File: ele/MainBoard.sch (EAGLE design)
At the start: 120 parts, among them IC1 MCP23017SP, IC2 74HC595D, IC3 74HC595D, X1 POWER_IN, X2 POWER_OUT

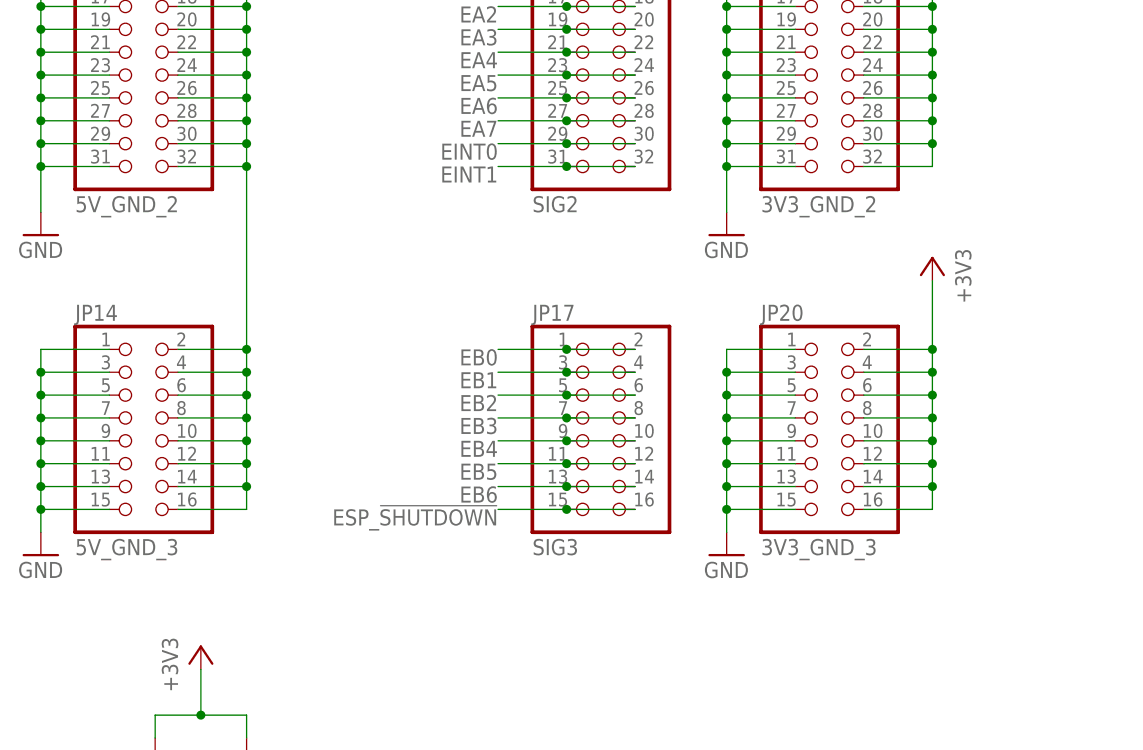
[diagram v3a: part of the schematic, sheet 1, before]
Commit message: ele: Remove impossible headers, route signals
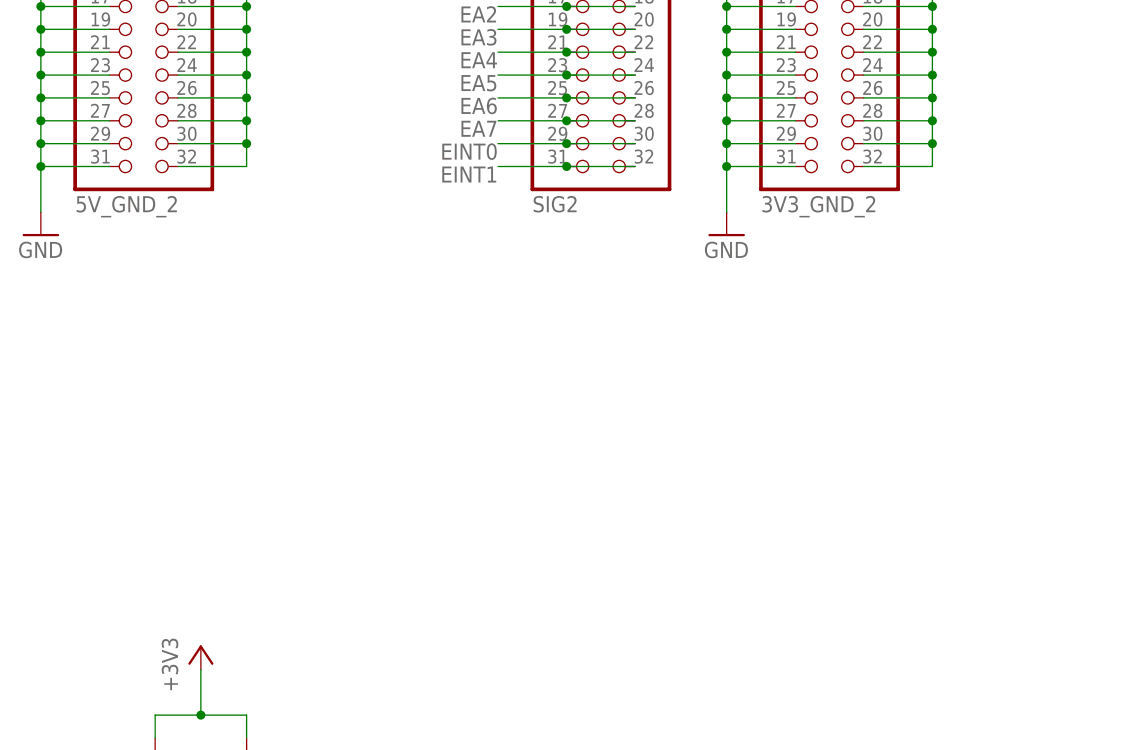
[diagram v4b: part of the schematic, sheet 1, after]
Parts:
- removed JP14: 5V_GND_3, pinhead:PINHD-2X8
- removed JP17: SIG3, pinhead:PINHD-2X8
- removed JP20: 3V3_GND_3, pinhead:PINHD-2X8
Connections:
- net +3V3: no longer JP20.10, JP20.12, JP20.14, JP20.16, JP20.2, JP20.4, JP20.6, JP20.8
- net 5V_2: no longer JP14.10, JP14.12, JP14.14, JP14.16, JP14.2, JP14.4, JP14.6, JP14.8
- net EB0: no longer JP17.1, JP17.2
- net EB1: no longer JP17.3, JP17.4
- net EB2: no longer JP17.5, JP17.6
- net EB3: no longer JP17.7, JP17.8
- net EB4: no longer JP17.10, JP17.9
- net EB5: no longer JP17.11, JP17.12
- net EB6: no longer JP17.13, JP17.14
- net ESP_!SHUTDOWN: no longer JP17.15, JP17.16
- net GND: no longer JP14.1, JP14.11, JP14.13, JP14.15, JP14.3, JP14.5, JP14.7, JP14.9, JP20.1, JP20.11, JP20.13, JP20.15, JP20.3, JP20.5, JP20.7, JP20.9

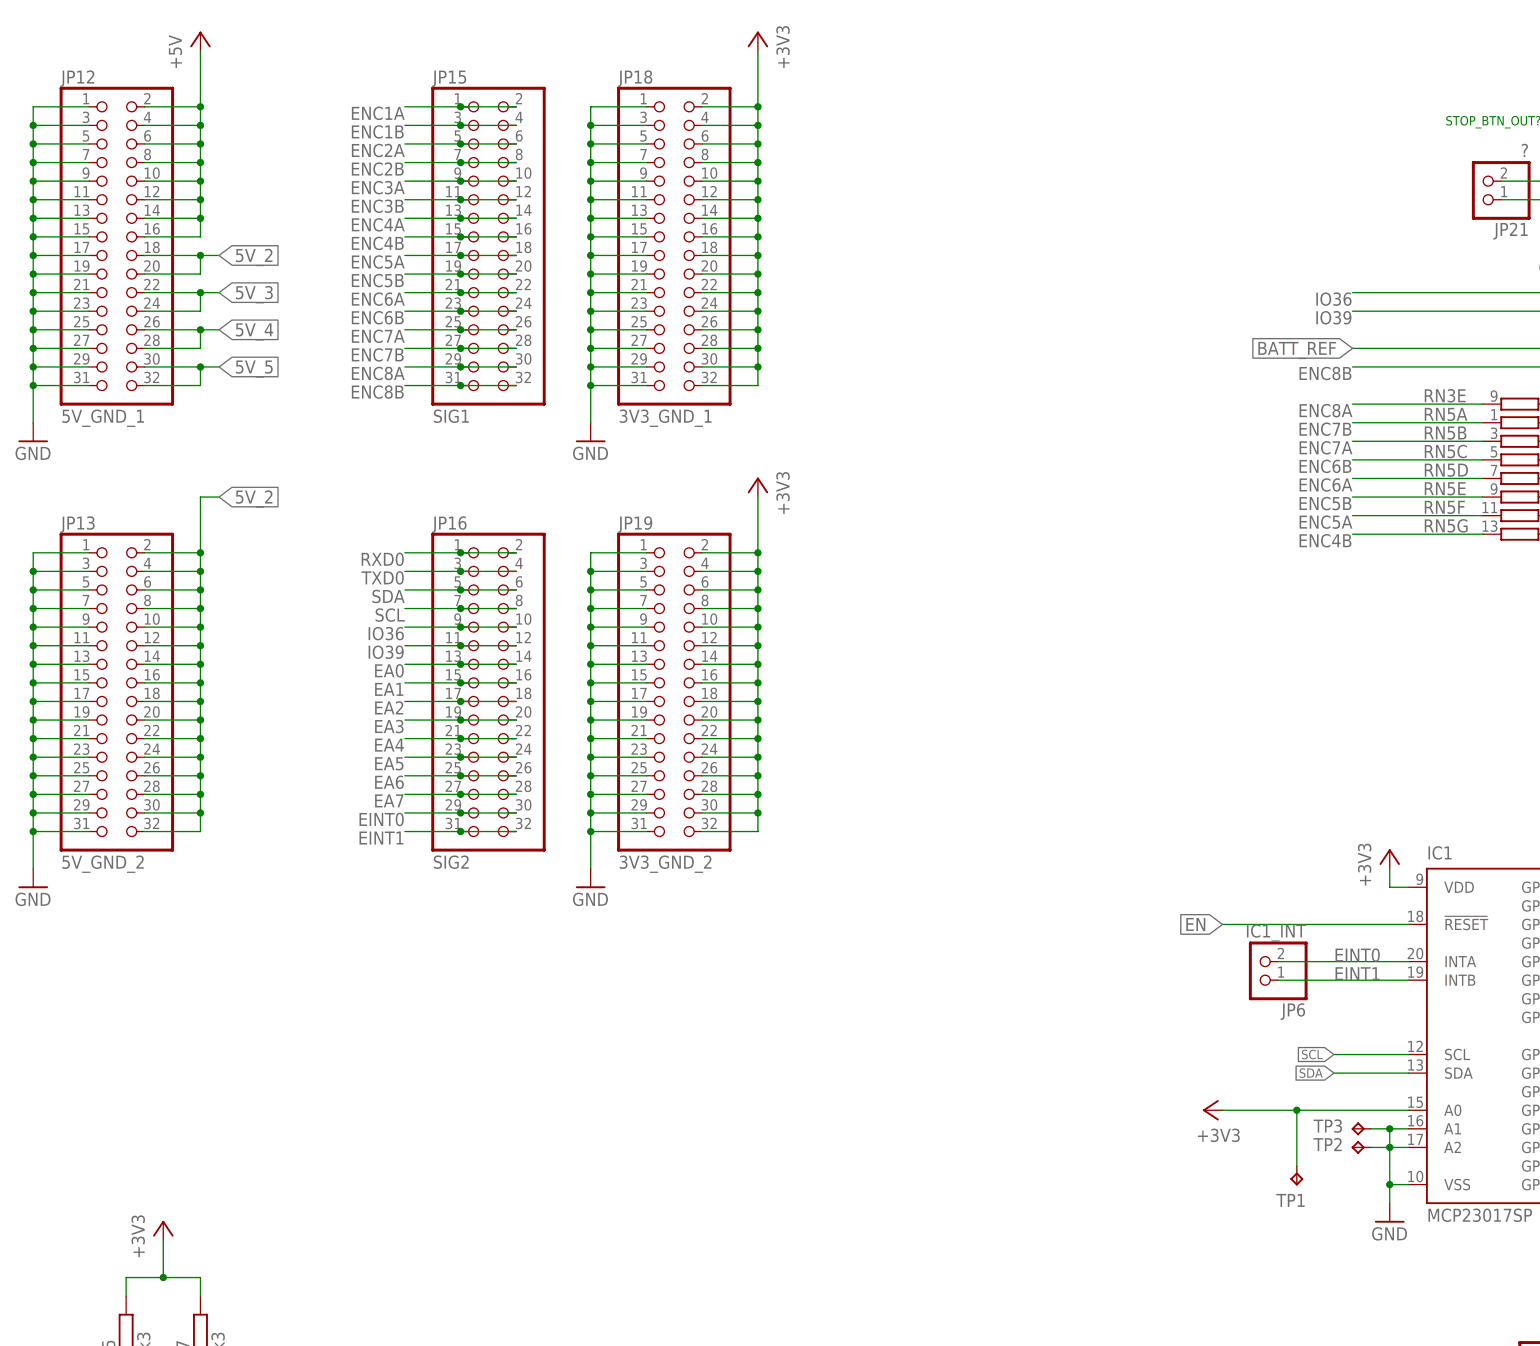
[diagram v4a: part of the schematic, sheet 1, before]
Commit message: ele: Return impossible headers, shrink board, route signals
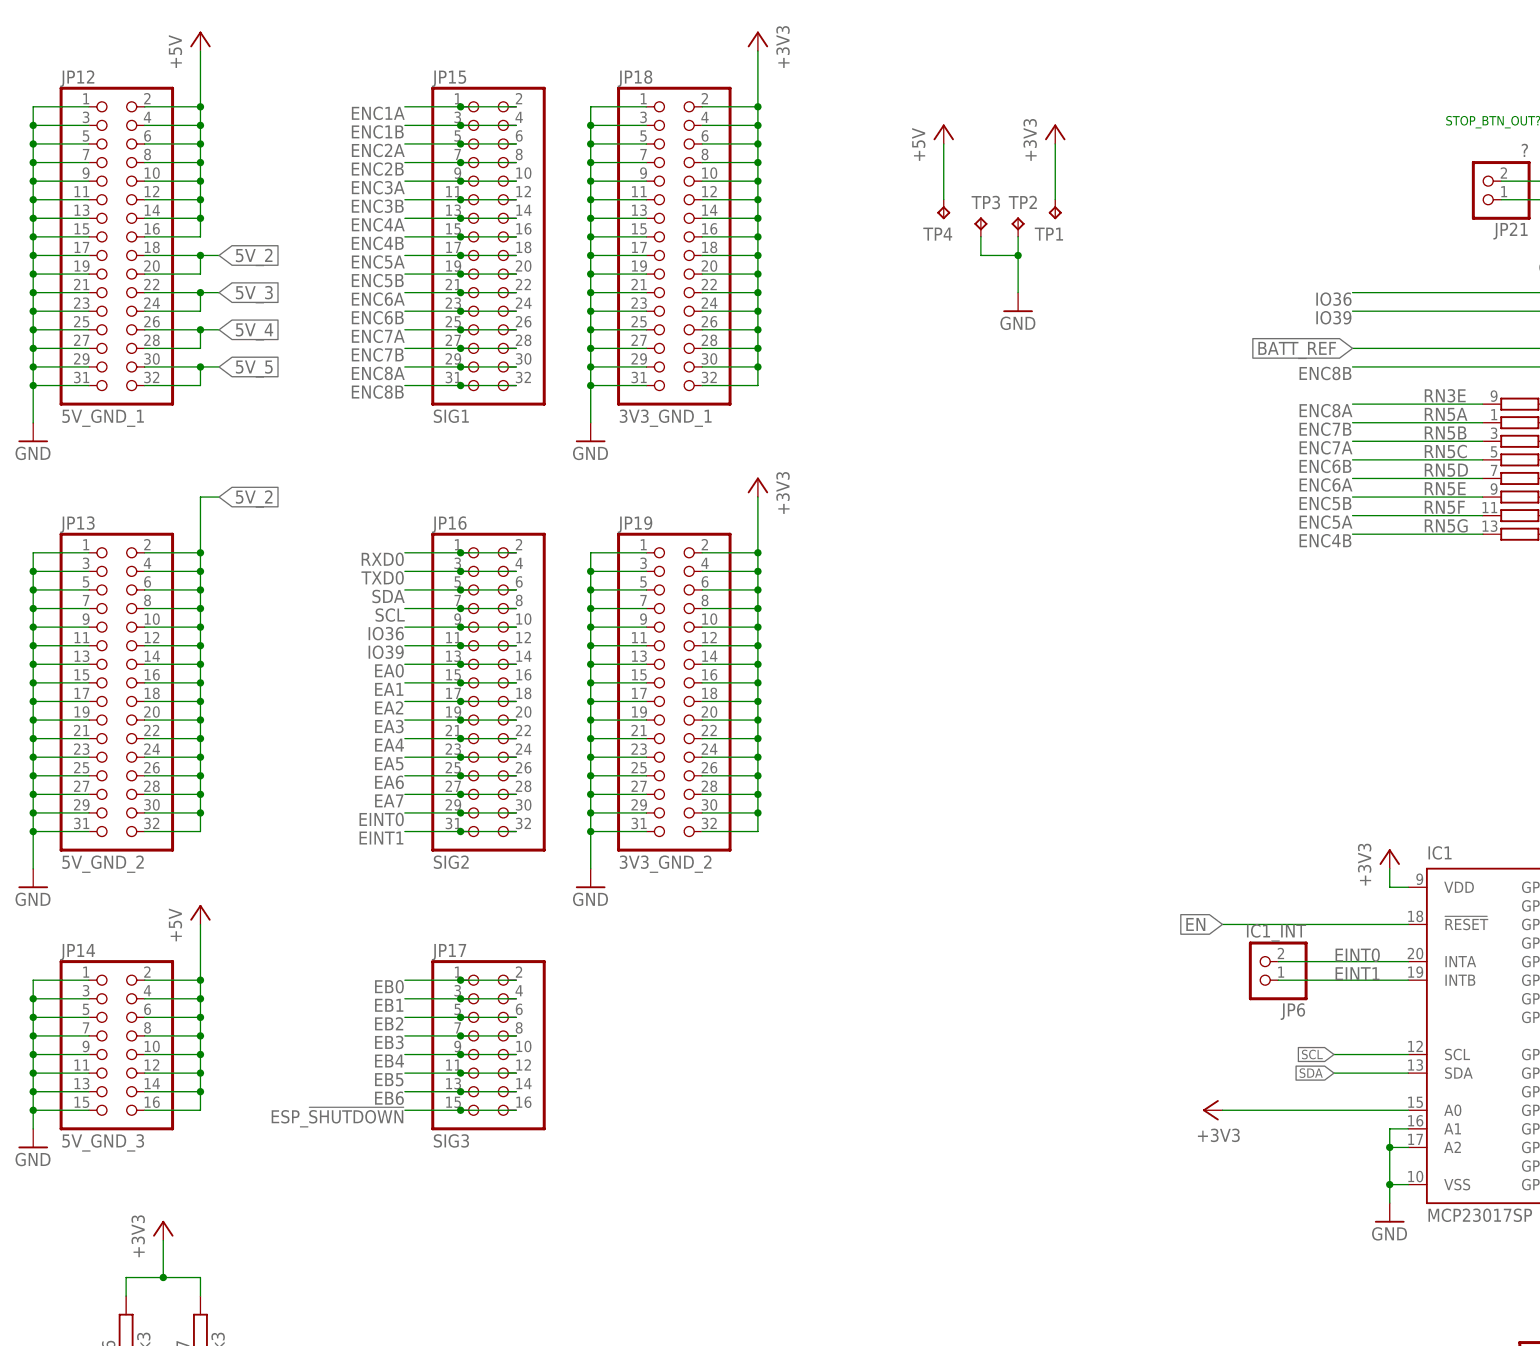
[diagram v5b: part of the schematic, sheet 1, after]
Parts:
- added JP14: 5V_GND_3, pinhead:PINHD-2X8
- added JP17: SIG3, pinhead:PINHD-2X8
- added TP4: TPTP20SQ, testpad:TPTP20SQ
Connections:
- net +5V: now also JP14.10, JP14.12, JP14.14, JP14.16, JP14.2, JP14.4, JP14.6, JP14.8, TP4.TP
- net EB0: now also JP17.1, JP17.2
- net EB1: now also JP17.3, JP17.4
- net EB2: now also JP17.5, JP17.6
- net EB3: now also JP17.7, JP17.8
- net EB4: now also JP17.10, JP17.9
- net EB5: now also JP17.11, JP17.12
- net EB6: now also JP17.13, JP17.14
- net ESP_!SHUTDOWN: now also JP17.15, JP17.16
- net GND: now also JP14.1, JP14.11, JP14.13, JP14.15, JP14.3, JP14.5, JP14.7, JP14.9
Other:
- moved on the sheet: TP1, TP2, TP3

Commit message: ele: Release Rev. A RC1
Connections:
- net 5V_2: no longer JP13.10, JP13.12, JP13.14, JP13.16, JP13.18, JP13.2, JP13.20, JP13.22, JP13.24, JP13.26, JP13.28, JP13.30, JP13.32, JP13.4, JP13.6, JP13.8
- net 5V_5: now also JP13.10, JP13.12, JP13.14, JP13.16, JP13.18, JP13.2, JP13.20, JP13.22, JP13.24, JP13.26, JP13.28, JP13.30, JP13.32, JP13.4, JP13.6, JP13.8

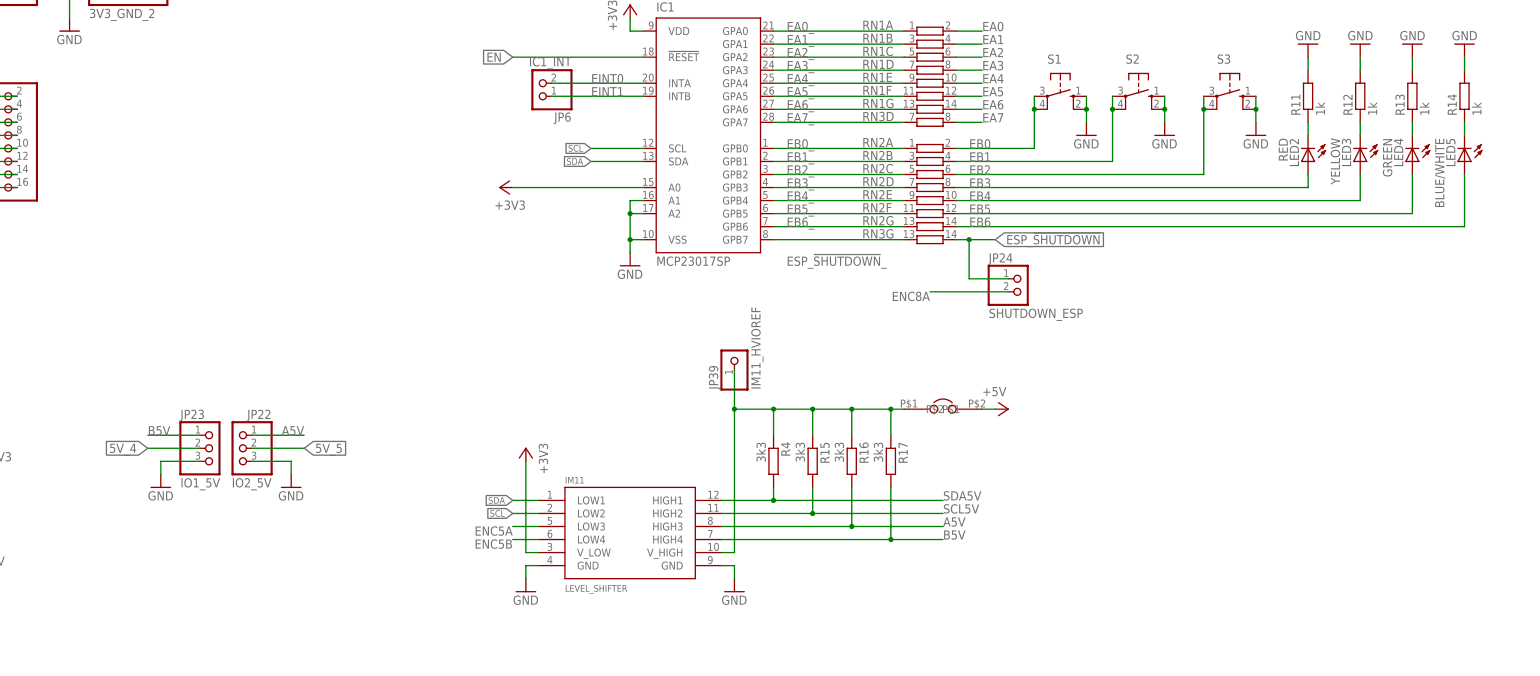
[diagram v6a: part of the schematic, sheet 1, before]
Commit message: Add licenses to Eagle files
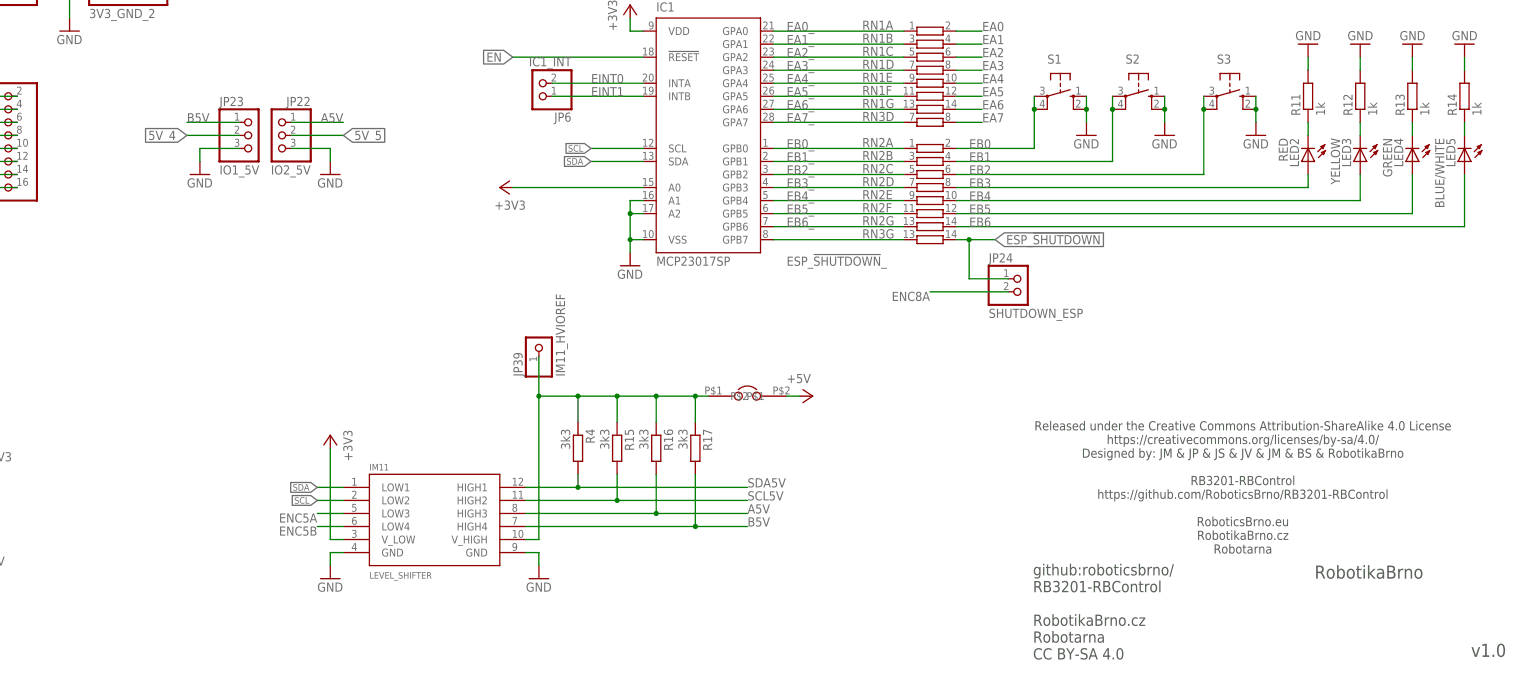
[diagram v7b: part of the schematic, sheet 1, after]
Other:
- note added: "Released under the Creative Commons Attribution-ShareAlike 4.0 License https://creativecommons.org/licenses/by-sa/4.0/ Designed by: JM & JP & JS & JV & JM & BS & RobotikaBrno RB3201-RBControl https://github.com/RoboticsBrno/RB3201-RBControl RoboticsBrno.eu RobotikaBrno.cz Robotarna"
- note added: "RobotikaBrno"
- note added: "github:roboticsbrno/ RB3201-RBControl RobotikaBrno.cz Robotarna CC BY-SA 4.0"
- note added: "v1.0"
- moved on the sheet: IM11, JP22, JP23, JP39, R15, R16, R17, R4

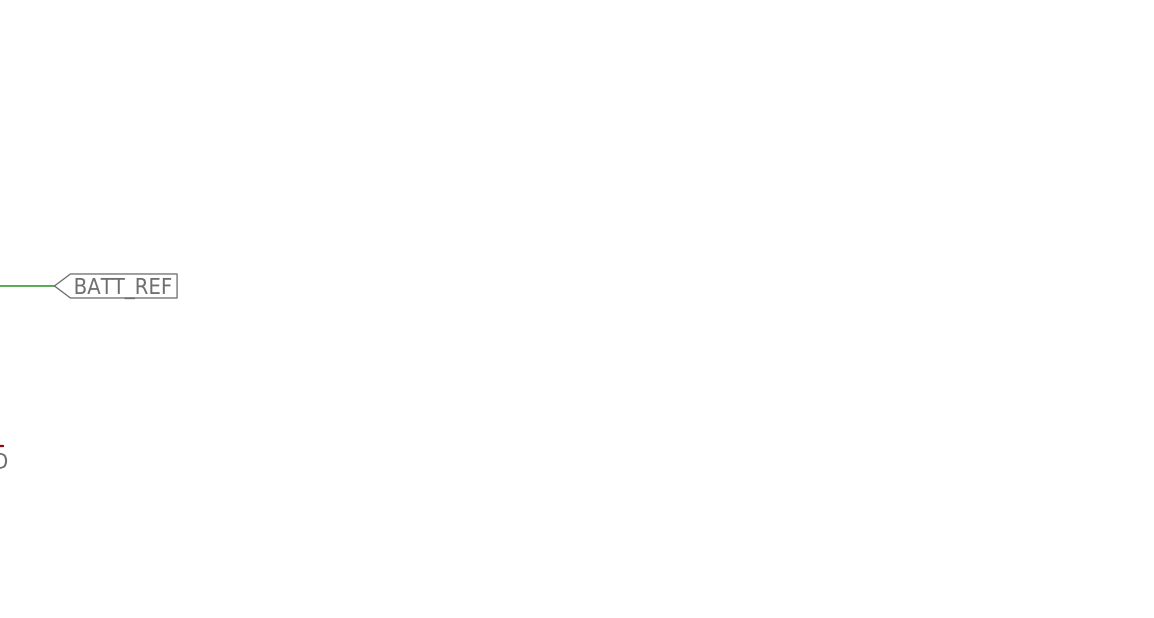
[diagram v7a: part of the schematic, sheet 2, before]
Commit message: ele: MainBoard - start work on v1.1 - make round corners (now just of left side)
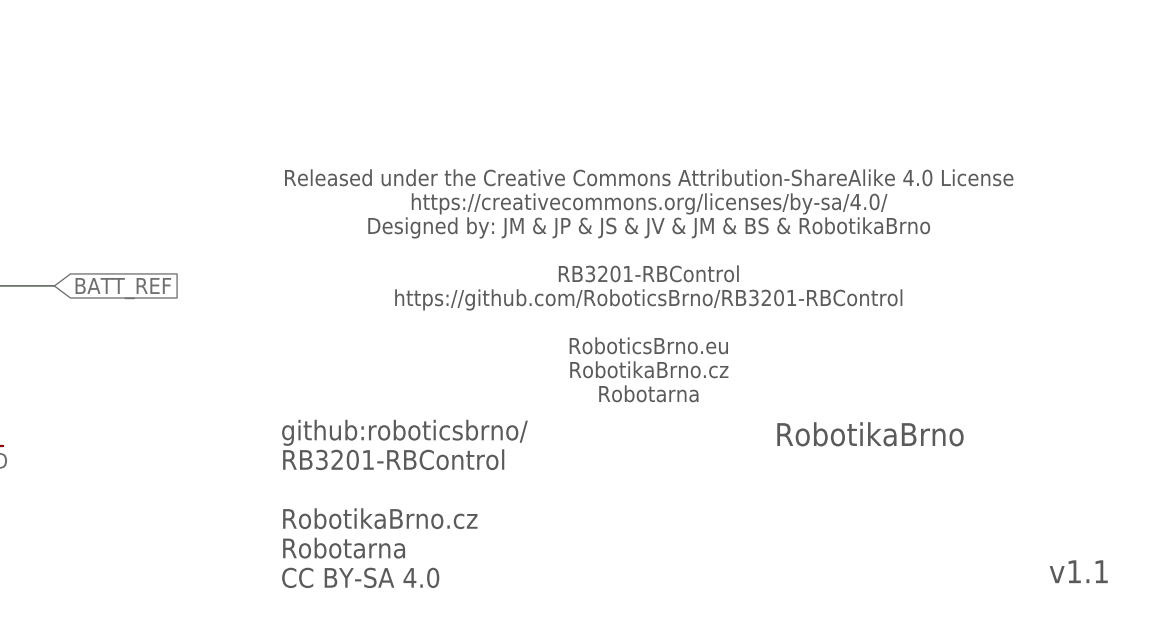
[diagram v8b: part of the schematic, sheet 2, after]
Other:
- note added: "v1.1"
- note removed: "v1.0"
